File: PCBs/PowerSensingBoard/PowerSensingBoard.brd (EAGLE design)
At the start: 100 x 80 mm, 12 parts

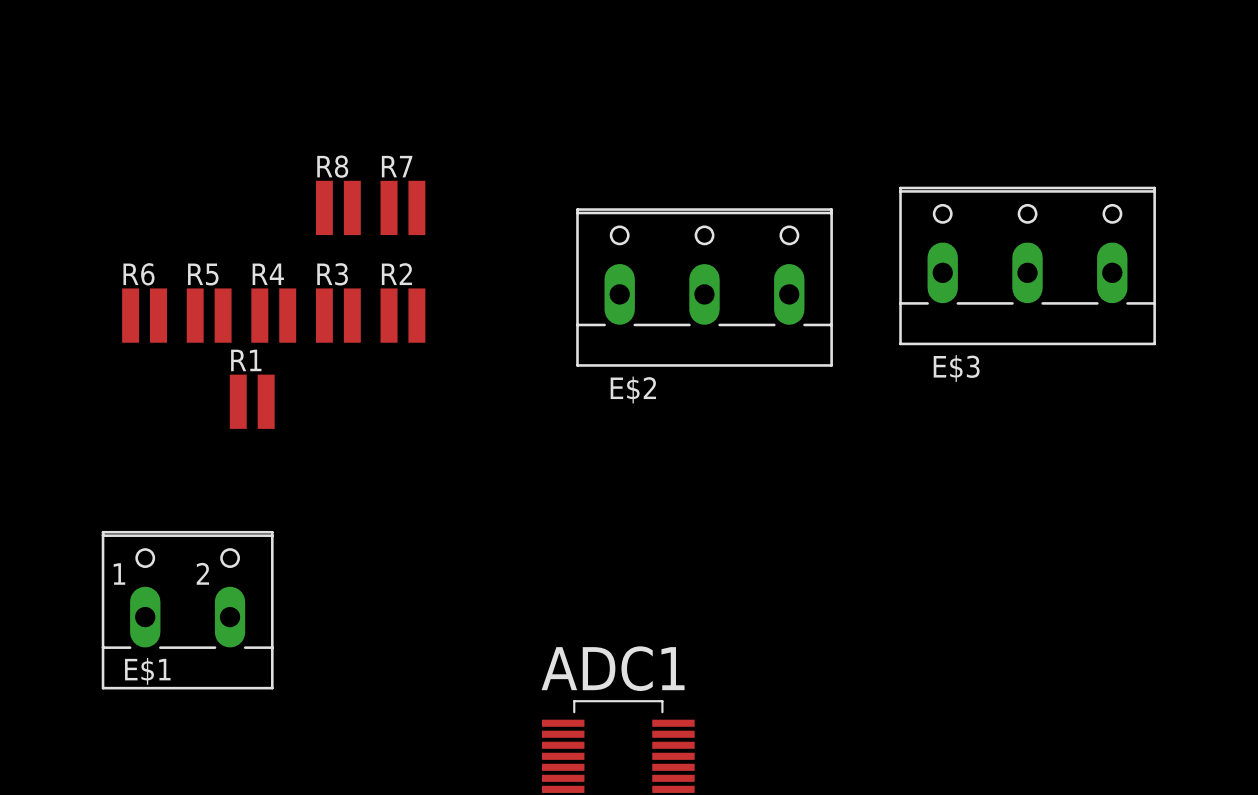
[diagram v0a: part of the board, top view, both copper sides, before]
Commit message: Adding prelim sensing schematic
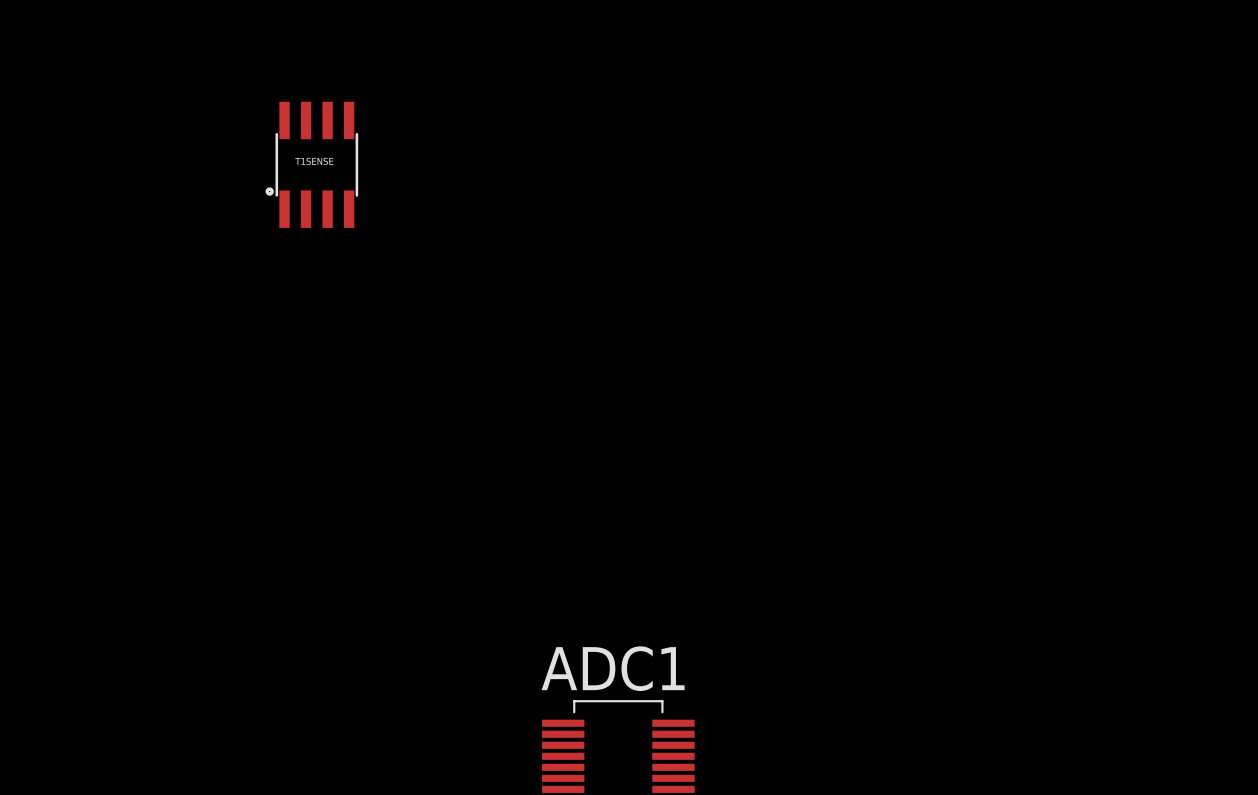
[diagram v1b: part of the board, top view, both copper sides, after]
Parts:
- removed E$1: (no value), con-wago-500:W237-102
- removed E$2, E$3: (no value), con-wago-500:W237-103
- removed R1, R2, R3, R4, R5, R6, R7, R8: (no value), resistor:PRL1632
- added T1SENSE: ACS712712SMD, SparkFun-AnalogIC:SO08
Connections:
- new net 5V: T1SENSE.8
- new net A0: T1SENSE.7
- new net FILT1: T1SENSE.6
- new net GND: T1SENSE.5
- new net T1IN: T1SENSE.1, T1SENSE.2
- new net T1OUT: T1SENSE.3, T1SENSE.4
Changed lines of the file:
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@@
 <layer number="48" name="Document" color="7" fill="1" visible="yes" active="yes"/>
 <layer number="49" name="Reference" color="7" fill="1" visible="yes" active="yes"/>
+<layer number="50" name="dxf" color="7" fill="1" visible="no" active="no"/>
 <layer number="51" name="tDocu" color="7" fill="1" visible="yes" active="yes"/>
 <layer number="52" name="bDocu" color="7" fill="1" visible="yes" active="yes"/>
+<layer number="53" name="tGND_GNDA" color="7" fill="9" visible="no" active="no"/>
+<layer number="54" name="bGND_GNDA" color="1" fill="9" visible="no" active="no"/>
+<layer number="56" name="wert" color="7" fill="1" visible="no" active="no"/>
+<layer number="57" name="tCAD" color="7" fill="1" visible="no" active="no"/>
+<layer number="59" name="tCarbon" color="7" fill="1" visible="no" active="no"/>
+<layer number="60" name="bCarbon" color="7" fill="1" visible="no" active="no"/>
 <layer number="90" name="Modules" color="5" fill="1" visible="no" active="no"/>
 <layer number="91" name="Nets" color="2" fill="1" visible="no" active="no"/>
@@
 <layer number="98" name="Guide" color="6" fill="1" visible="no" active="no"/>
 <layer number="99" name="SpiceOrder" color="5" fill="1" visible="no" active="no"/>
+<layer number="100" name="Muster" color="7" fill="1" visible="no" active="no"/>
+<layer number="101" name="Patch_Top" color="12" fill="4" visible="yes" active="yes"/>
+<layer number="102" name="Vscore" color="7" fill="1" visible="yes" active="yes"/>
+<layer number="103" name="tMap" color="7" fill="1" visible="yes" active="yes"/>
+<layer number="104" name="Name" color="16" fill="1" visible="yes" active="yes"/>
+<layer number="105" name="tPlate" color="7" fill="1" visible="yes" active="yes"/>
+<layer number="106" name="bPlate" color="7" fill="1" visible="yes" active="yes"/>
+<layer number="107" name="Crop" color="7" fill="1" visible="yes" active="yes"/>
+<layer number="108" name="tplace-old" color="10" fill="1" visible="yes" active="yes"/>
+<layer number="109" name="ref-old" color="11" fill="1" visible="yes" active="yes"/>
+<layer number="110" name="fp0" color="7" fill="1" visible="yes" active="yes"/>
+<layer number="111" name="LPC17xx" color="7" fill="1" visible="yes" active="yes"/>
+<layer number="112" name="tSilk" color="7" fill="1" visible="yes" active="yes"/>
+<layer number="113" name="IDFDebug" color="7" fill="1" visible="yes" active="yes"/>
+<layer number="116" name="Patch_BOT" color="9" fill="4" visible="yes" active="yes"/>
+<layer number="118" name="Rect_Pads" color="7" fill="1" visible="yes" active="yes"/>
+<layer number="121" name="_tsilk" color="7" fill="1" visible="yes" active="yes"/>
+<layer number="122" name="_bsilk" color="7" fill="1" visible="yes" active="yes"/>
+<layer number="123" name="tTestmark" color="7" fill="1" visible="yes" active="yes"/>
+<layer number="124" name="bTestmark" color="7" fill="1" visible="yes" active="yes"/>
+<layer number="125" name="_tNames" color="7" fill="1" visible="yes" active="yes"/>
+<layer number="126" name="_bNames" color="7" fill="1" visible="yes" active="yes"/>
+<layer number="127" name="_tValues" color="7" fill="1" visible="yes" active="yes"/>
+<layer number="128" name="_bValues" color="7" fill="1" visible="yes" active="yes"/>
+<layer number="129" name="Mask" color="7" fill="1" visible="yes" active="yes"/>
+<layer number="131" name="tAdjust" color="7" fill="1" visible="yes" active="yes"/>
+<layer number="132" name="bAdjust" color="7" fill="1" visible="yes" active="yes"/>
+<layer number="144" name="Drill_legend" color="7" fill="1" visible="yes" active="yes"/>
+<layer number="150" name="Notes" color="7" fill="1" visible="yes" active="yes"/>
+<layer number="151" name="HeatSink" color="7" fill="1" visible="yes" active="yes"/>
+<layer number="152" name="_bDocu" color="7" fill="1" visible="yes" active="yes"/>
+<layer number="153" name="FabDoc1" color="7" fill="1" visible="yes" active="yes"/>
+<layer number="154" name="FabDoc2" color="7" fill="1" visible="yes" active="yes"/>
+<layer number="155" name="FabDoc3" color="7" fill="1" visible="yes" active="yes"/>
+<layer number="199" name="Contour" color="7" fill="1" visible="yes" active="yes"/>
+<layer number="200" name="200bmp" color="1" fill="10" visible="yes" active="yes"/>
+<layer number="201" name="201bmp" color="2" fill="10" visible="yes" active="yes"/>
+<layer number="202" name="202bmp" color="3" fill="10" visible="yes" active="yes"/>
+<layer number="203" name="203bmp" color="4" fill="10" visible="yes" active="yes"/>
+<layer number="204" name="204bmp" color="5" fill="10" visible="yes" active="yes"/>
+<layer number="205" name="205bmp" color="6" fill="10" visible="yes" active="yes"/>
+<layer number="206" name="206bmp" color="7" fill="10" visible="yes" active="yes"/>
+<layer number="207" name="207bmp" color="8" fill="10" visible="yes" active="yes"/>
+<layer number="208" name="208bmp" color="9" fill="10" visible="yes" active="yes"/>
+<layer number="209" name="209bmp" color="7" fill="1" visible="yes" active="yes"/>
+<layer number="210" name="210bmp" color="7" fill="1" visible="yes" active="yes"/>
+<layer number="211" name="211bmp" color="7" fill="1" visible="yes" active="yes"/>
+<layer number="212" name="212bmp" color="7" fill="1" visible="yes" active="yes"/>
+<layer number="213" name="213bmp" color="7" fill="1" visible="yes" active="yes"/>
+<layer number="214" name="214bmp" color="7" fill="1" visible="yes" active="yes"/>
+<layer number="215" name="215bmp" color="7" fill="1" visible="yes" active="yes"/>
+<layer number="216" name="216bmp" color="7" fill="1" visible="yes" active="yes"/>
+<layer number="217" name="217bmp" color="18" fill="1" visible="no" active="no"/>
+<layer number="218" name="218bmp" color="19" fill="1" visible="no" active="no"/>
+<layer number="219" name="219bmp" color="20" fill="1" visible="no" active="no"/>
+<layer number="220" name="220bmp" color="21" fill="1" visible="no" active="no"/>
+<layer number="221" name="221bmp" color="22" fill="1" visible="no" active="no"/>
+<layer number="222" name="222bmp" color="23" fill="1" visible="no" active="no"/>
+<layer number="223" name="223bmp" color="24" fill="1" visible="no" active="no"/>
+<layer number="224" name="224bmp" color="25" fill="1" visible="no" active="no"/>
+<layer number="225" name="225bmp" color="7" fill="1" visible="yes" active="yes"/>
+<layer number="226" name="226bmp" color="7" fill="1" visible="yes" active="yes"/>
+<layer number="227" name="227bmp" color="7" fill="1" visible="yes" active="yes"/>
+<layer number="228" name="228bmp" color="7" fill="1" visible="yes" active="yes"/>
+<layer number="229" name="229bmp" color="7" fill="1" visible="yes" active="yes"/>
+<layer number="230" name="230bmp" color="7" fill="1" visible="yes" active="yes"/>
+<layer number="231" name="231bmp" color="7" fill="1" visible="yes" active="yes"/>
+<layer number="248" name="Housing" color="7" fill="1" visible="yes" active="yes"/>
+<layer number="249" name="Edge" color="7" fill="1" visible="yes" active="yes"/>
+<layer number="250" name="Descript" color="3" fill="1" visible="no" active="no"/>
+<layer number="251" name="SMDround" color="12" fill="11" visible="no" active="no"/>
+<layer number="254" name="cooling" color="7" fill="1" visible="yes" active="yes"/>
+<layer number="255" name="routoute" color="7" fill="1" visible="yes" active="yes"/>
 </layers>
 <board>
@@
 </autorouter>
 <elements>
-<element name="R1" library="resistor" package="PRL1632" value="" x="19.05" y="41.91"/>
-<element name="R2" library="resistor" package="PRL1632" value="" x="27.94" y="46.99"/>
-<element name="R3" library="resistor" package="PRL1632" value="" x="24.13" y="46.99"/>
-<element name="R4" library="resistor" package="PRL1632" value="" x="20.32" y="46.99"/>
-<element name="R5" library="resistor" package="PRL1632" value="" x="16.51" y="46.99"/>
-<element name="R6" library="resistor" package="PRL1632" value="" x="12.7" y="46.99"/>
-<element name="R7" library="resistor" package="PRL1632" value="" x="27.94" y="53.34"/>
-<element name="R8" library="resistor" package="PRL1632" value="" x="24.13" y="53.34"/>
 <element name="ADC1" library="HostlerLib" package="SSOP-28" value="LTC1856SSOP28" x="40.64" y="19.05"/>
-<element name="E$1" library="con-wago-500" package="W237-102" value="" x="15.24" y="30.48"/>
-<element name="E$2" library="con-wago-500" package="W237-103" value="" x="45.72" y="49.53"/>
-<element name="E$3" library="con-wago-500" package="W237-103" value="" x="64.77" y="50.8"/>
+<element name="T1SENSE" library="SparkFun-AnalogIC" package="SO08" value="ACS712712SMD" x="22.86" y="55.88">
+<attribute name="PROD_ID" value="IC-08964" x="22.86" y="55.88" size="1.778" layer="27" display="off"/>
+</element>
 </elements>
 <signals>
+<signal name="T1IN">
+<contactref element="T1SENSE" pad="1"/>
+<contactref element="T1SENSE" pad="2"/>
+<wire x1="22.225" y1="53.2638" x2="20.955" y2="53.2638" width="0" layer="19" extent="1-1"/>
+</signal>
+<signal name="T1OUT">
+<contactref element="T1SENSE" pad="3"/>
+<contactref element="T1SENSE" pad="4"/>
+<wire x1="24.765" y1="53.2638" x2="23.495" y2="53.2638" width="0" layer="19" extent="1-1"/>
+</signal>
+<signal name="5V">
+<contactref element="T1SENSE" pad="8"/>
+</signal>
+<signal name="A0">
+<contactref element="T1SENSE" pad="7"/>
+</signal>
+<signal name="FILT1">
+<contactref element="T1SENSE" pad="6"/>
+</signal>
+<signal name="GND">
+<contactref element="T1SENSE" pad="5"/>
+</signal>
 </signals>
 </board>

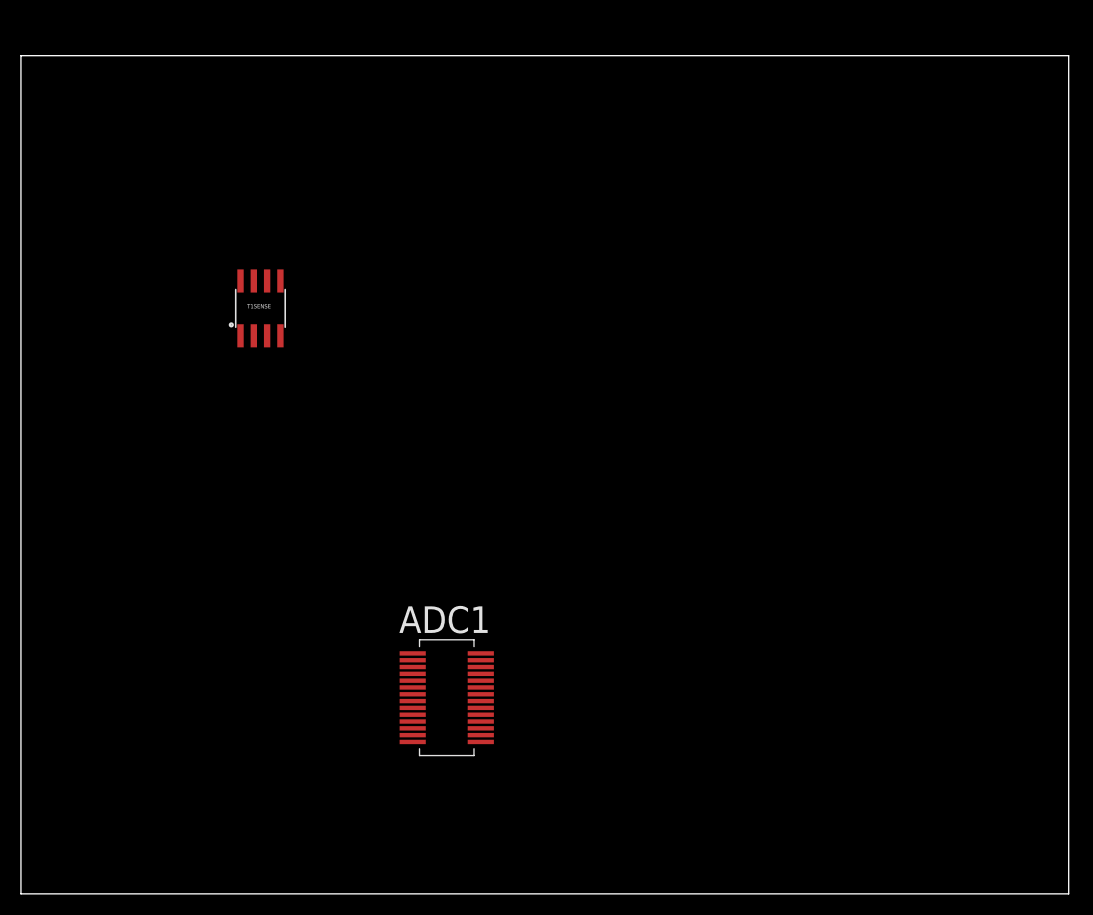
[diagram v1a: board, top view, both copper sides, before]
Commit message: Power Sensing board design
Power sensing rough draft of PCB almost done
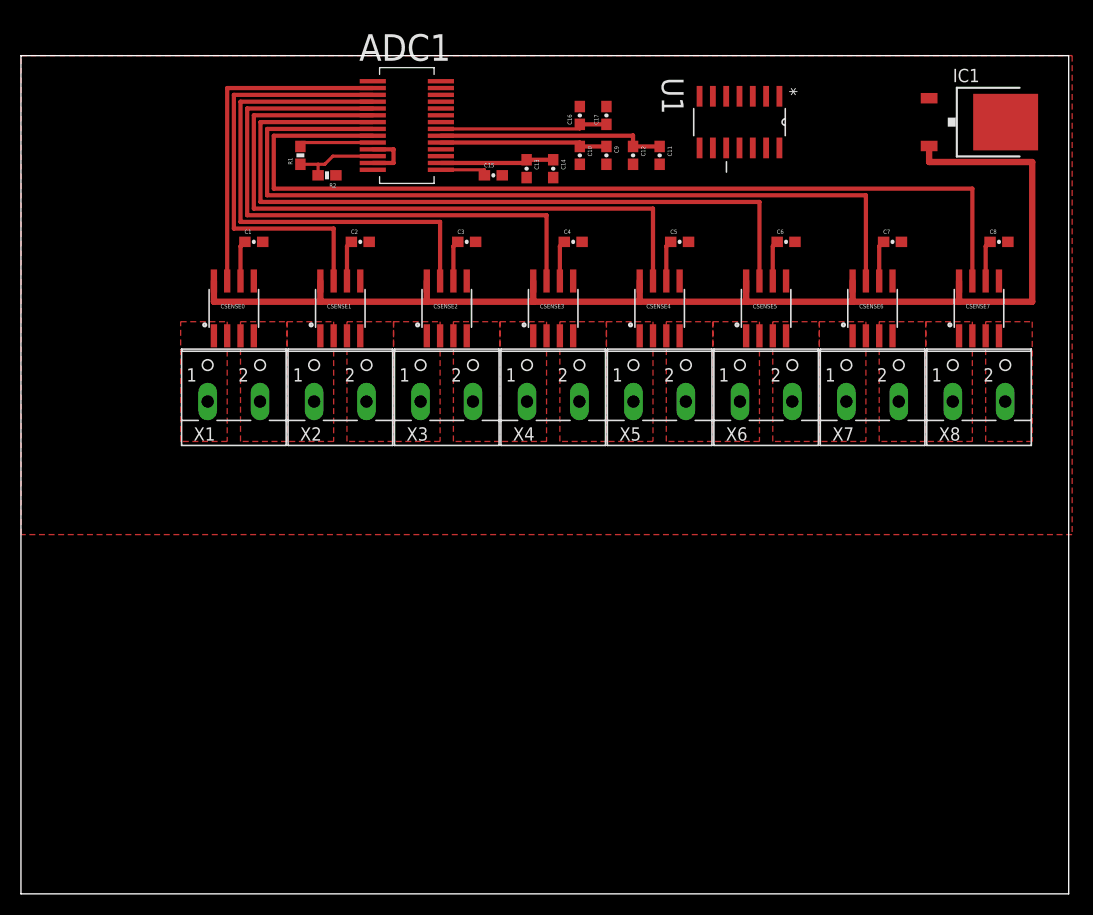
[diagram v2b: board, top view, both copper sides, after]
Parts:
- removed T1SENSE: ACS712712SMD, SparkFun-AnalogIC:SO08
- added C1, C2, C3, C4, C5, C6, C7, C8: 4.7uF, SparkFun-Capacitors:0603-CAP
- added C10, C12, C14, C17: 10uF, SparkFun-Capacitors:0603-CAP
- added C11, C13, C16, C9: .1uF, SparkFun-Capacitors:0603-CAP
- added C15: 1uF, SparkFun-Capacitors:0603-CAP
- added CSENSE0, CSENSE1, CSENSE2, CSENSE3, CSENSE4, CSENSE5, CSENSE6, CSENSE7: ACS712712SMD, SparkFun-AnalogIC:SO08
- added IC1: 7805DT, adafruit:TO252
- added R1: 1.5K, SparkFun-Resistors:0603-RES
- added R2: 1K, SparkFun-Resistors:0603-RES
- added U1: ATTINY84-20SSU, Atmel_By_element14_Batch_1-00:SOIC127P600X175-14N
- added X1, X2, X3, X4, X5, X6, X7, X8: (no value), con-wago-500:W237-102
- moved ADC1 54.7 mm to (36.8, 73.7)
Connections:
- removed net T1IN: T1SENSE.1, T1SENSE.2
- removed net T1OUT: T1SENSE.3, T1SENSE.4
- new net A1: ADC1.3, CSENSE1.7
- new net A2: ADC1.4, CSENSE2.7
- new net A3: ADC1.5, CSENSE3.7
- new net A4: ADC1.6, CSENSE4.7
- new net A5: ADC1.7, CSENSE5.7
- new net A6: ADC1.8, CSENSE6.7
- new net A7: ADC1.9, CSENSE7.7
- new net CLK: ADC1.26, U1.9
- new net CONVST: ADC1.28
- new net FILT2: C2.1, CSENSE1.6
- new net FILT3: C3.1, CSENSE2.6
- new net FILT4: C4.1, CSENSE3.6
- new net FILT5: C5.1, CSENSE4.6
- new net FILT6: C6.1, CSENSE5.6
- new net FILT7: C7.1, CSENSE6.6
- new net FILT8: C8.1, CSENSE7.6
- new net INT1: CSENSE0.1, CSENSE0.2, X1.1
- new net INT2: CSENSE1.1, CSENSE1.2, X2.1
- new net INT3: CSENSE2.1, CSENSE2.2, X3.1
- new net INT4: CSENSE3.1, CSENSE3.2, X4.1
- new net INT5: CSENSE4.1, CSENSE4.2, X5.1
- new net INT6: CSENSE5.1, CSENSE5.2, X6.1
- new net INT7: CSENSE6.1, CSENSE6.2, X7.1
- new net INT8: CSENSE7.1, CSENSE7.2, X8.1
- new net MISO: ADC1.23, U1.8
- new net MOSI: ADC1.25, U1.7
- new net N$1: U1.5
- new net N$10: ADC1.20, C11.1, C12.1
- new net N$11: ADC1.19, C10.1, C9.1
- new net N$12: ADC1.15, C15.1
- new net N$13: ADC1.16, C13.1, C14.1
- new net N$14: U1.6
- new net N$16: IC1.1
- new net N$17: IC1.3
- new net N$2: ADC1.10, R1.2
- new net N$3: ADC1.12, R1.1, R2.2
- new net N$4: U1.14
- new net N$5: ADC1.11, ADC1.13
- new net N$6: U1.13
- new net N$7: U1.12
- new net N$8: U1.11
- new net OUTT1: CSENSE0.3, CSENSE0.4, X1.2
- new net OUTT2: CSENSE1.3, CSENSE1.4, X2.2
- new net OUTT3: CSENSE2.3, CSENSE2.4, X3.2
- new net OUTT4: CSENSE3.3, CSENSE3.4, X4.2
- new net OUTT5: CSENSE4.3, CSENSE4.4, X5.2
- new net OUTT6: CSENSE5.3, CSENSE5.4, X6.2
- new net OUTT7: CSENSE6.3, CSENSE6.4, X7.2
- new net OUTT8: CSENSE7.3, CSENSE7.4, X8.2
- new net RST: U1.4
- new net RX: U1.3
- new net TX: U1.2
- new net ~BUSY: ADC1.22, U1.10
- new net ~RD: ADC1.27
- net 5V: now also ADC1.21, C16.1, C17.1, CSENSE0.8, CSENSE1.8, CSENSE2.8, CSENSE3.8, CSENSE4.8, CSENSE5.8, CSENSE6.8, CSENSE7.8, IC1.2, U1.1; no longer T1SENSE.8
- net A0: now also ADC1.2, CSENSE0.7; no longer T1SENSE.7
- net FILT1: now also C1.1, CSENSE0.6; no longer T1SENSE.6
- net GND: now also ADC1.1, ADC1.14, ADC1.17, ADC1.18, ADC1.24, C1.2, C10.2, C11.2, C12.2, C13.2, C14.2, C15.2, C16.2, C17.2, C2.2, C3.2, C4.2, C5.2, C6.2, C7.2, C8.2, C9.2, CSENSE0.5, CSENSE1.5, CSENSE2.5, CSENSE3.5, CSENSE4.5, CSENSE5.5, CSENSE6.5, CSENSE7.5, R2.1; no longer T1SENSE.5
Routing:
- net 5V: track 0.00 -> 134.9 mm
- net A7: track 0.00 -> 90.0 mm
- net A6: track 0.00 -> 81.7 mm
- net A5: track 0.00 -> 73.5 mm
- net A4: track 0.00 -> 65.3 mm
- net A3: track 0.00 -> 57.0 mm
- net A2: track 0.00 -> 48.8 mm
- net A1: track 0.00 -> 40.5 mm
- net A0: track 0.00 -> 32.3 mm
- net N$10: track 0.00 -> 21.9 mm
- net N$11: track 0.00 -> 16.2 mm
- net N$13: track 0.00 -> 11.0 mm
- net N$3: track 0.00 -> 8.29 mm
- net N$2: track 0.00 -> 7.28 mm
- net N$5: track 0.00 -> 5.26 mm
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- added copper zone on layer 1, net GND
- added copper zone on layer 1, net INT1
- added copper zone on layer 1, net INT2
- added copper zone on layer 1, net INT3
- added copper zone on layer 1, net INT4
- added copper zone on layer 1, net INT5
- added copper zone on layer 1, net INT6
- added copper zone on layer 1, net INT7
- added copper zone on layer 1, net INT8
- added copper zone on layer 1, net OUTT1
- added copper zone on layer 1, net OUTT2
- added copper zone on layer 1, net OUTT3
- added copper zone on layer 1, net OUTT4
- added copper zone on layer 1, net OUTT5
- added copper zone on layer 1, net OUTT6
- added copper zone on layer 1, net OUTT7
- added copper zone on layer 1, net OUTT8
